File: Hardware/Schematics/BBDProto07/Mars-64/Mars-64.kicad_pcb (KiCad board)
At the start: 4 copper layers, 45.7 x 101.6 mm, 79 parts, among them J101 Conn_Coaxial, J102 Conn_Coaxial, U101 ADG731, U102 ADG731

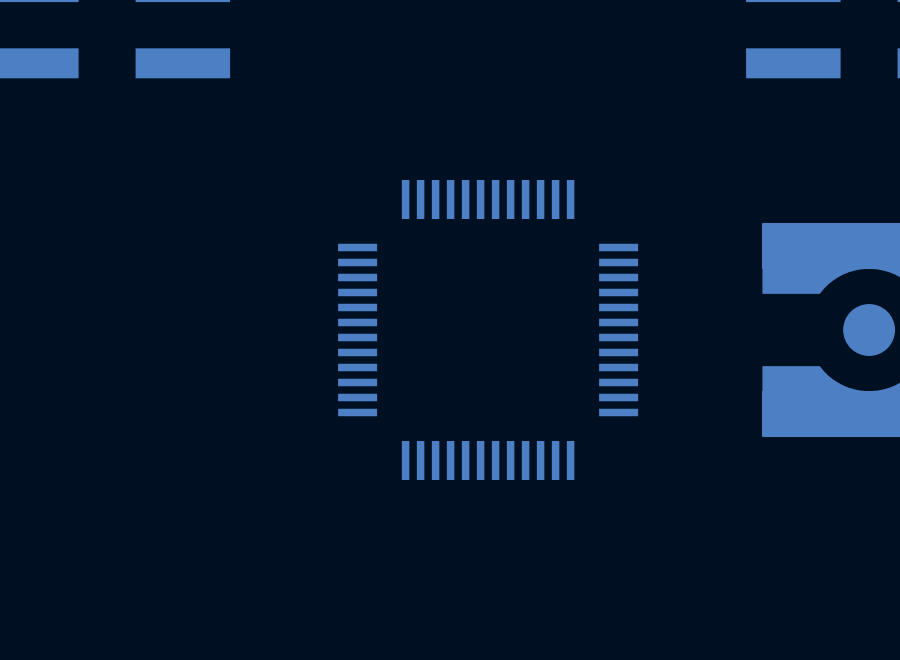
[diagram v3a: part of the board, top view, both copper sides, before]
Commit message: Completed the autorouting for the U101 rotations
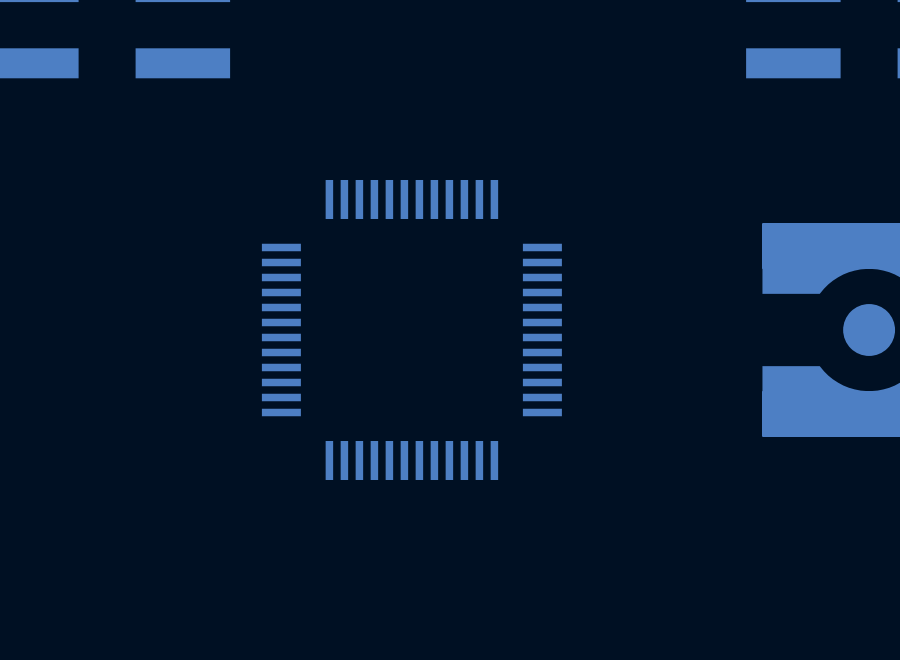
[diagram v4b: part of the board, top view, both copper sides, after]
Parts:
- moved U101 2.54 mm to (78.7, 68.6)
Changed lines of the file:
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@@
   )
   (module Package_QFP:TQFP-48_7x7mm_P0.5mm (layer B.Cu)
-    (at 81.28 68.58 180)
+    (at 78.74 68.58 180)
     (descr "48 LEAD TQFP 7x7mm (see MICREL TQFP7x7-48LD-PL-1.pdf)")
     (tags "QFP 0.5")

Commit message: Added the new fabrication files
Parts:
- turned U102 to 180 degrees
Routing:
- net Net-(JP5-Pad2): track 0.00 -> 204.3 mm
- net /VCC3V3: track 0.00 -> 184.6 mm, vias 0 -> 4
- net /SPI_CLK: track 0.00 -> 184.0 mm, vias 0 -> 2
- net GND: track 0.00 -> 170.6 mm, vias 0 -> 2
- net /SPI_MOSI: track 0.00 -> 139.6 mm
- net /~SPI_CE: track 0.00 -> 134.1 mm
- net Net-(J101-Pad2): track 0.00 -> 124.4 mm, vias 0 -> 2
- net /DB: track 0.00 -> 108.6 mm, vias 0 -> 2
- net Net-(TP204-Pad1): track 0.00 -> 65.9 mm
- net Net-(TP210-Pad1): track 0.00 -> 61.2 mm
- net Net-(TP131-Pad1): track 0.00 -> 60.8 mm, vias 1 -> 2
- net Net-(TP205-Pad1): track 0.00 -> 59.1 mm
- net Net-(TP132-Pad1): track 0.00 -> 58.3 mm
- net Net-(TP208-Pad1): track 0.00 -> 56.4 mm
- net Net-(TP129-Pad1): track 0.00 -> 55.8 mm, vias 1 -> 2
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
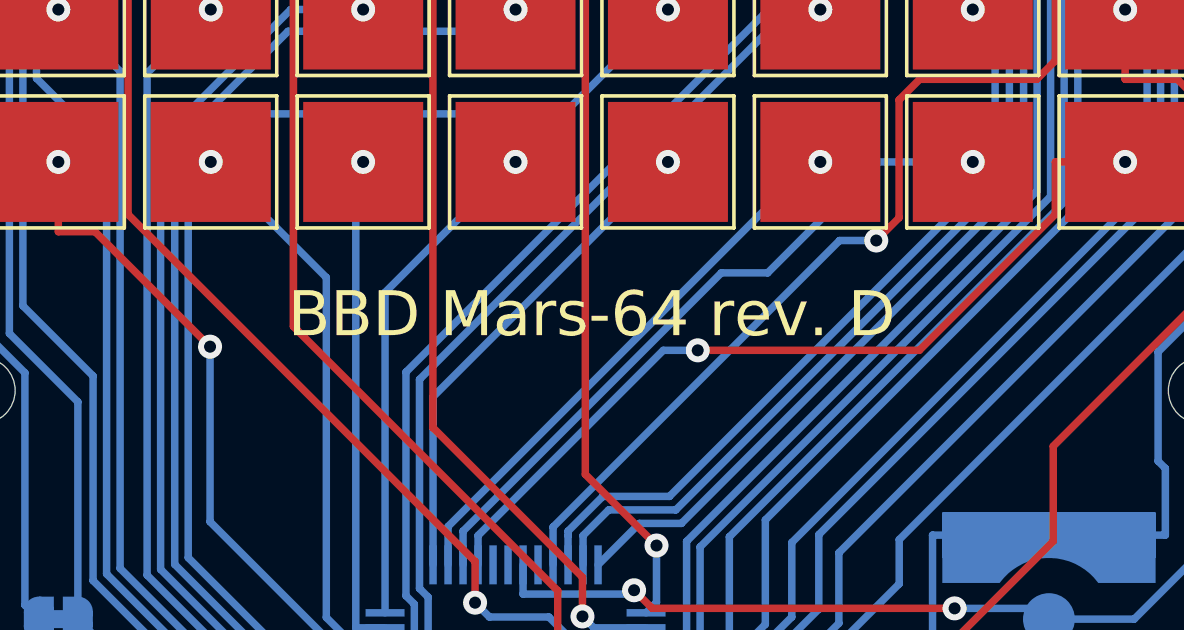
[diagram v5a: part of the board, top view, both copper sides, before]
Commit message: Fixed a few bugs on the PCB and changed the revision from D to E
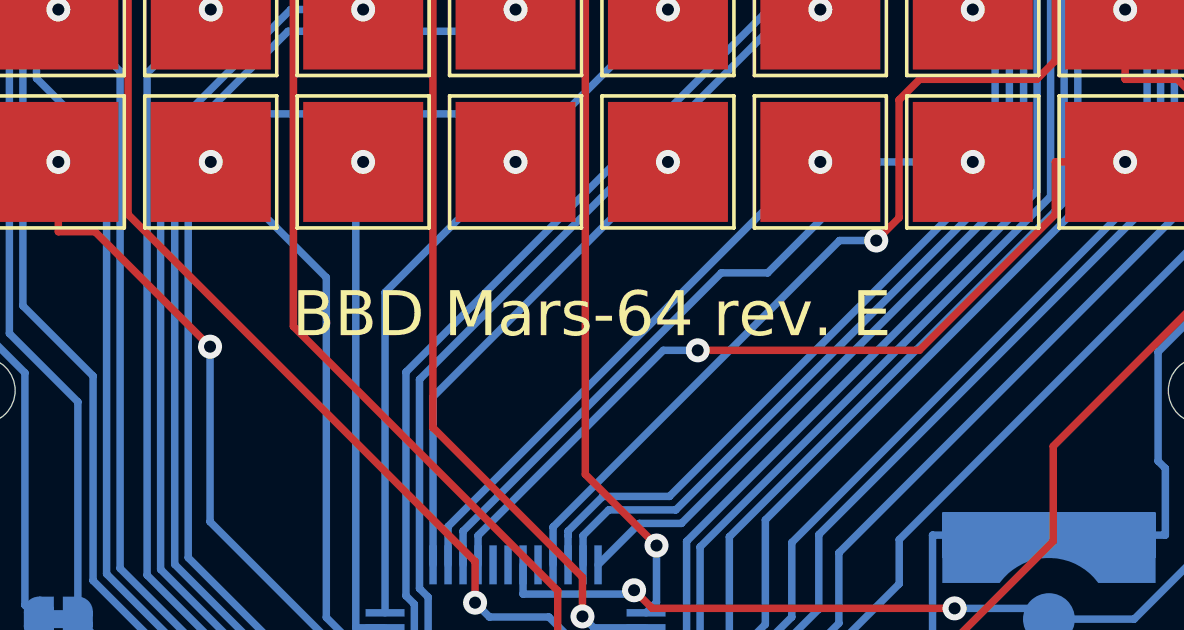
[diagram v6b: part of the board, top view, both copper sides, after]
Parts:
- removed PmodF2: Conn_02x06_Top_Bottom, Mars-64:PinHeader_2x06_P2.54mm_Vertical_SMD_TopBottom_Mirrored
- added PmodF: Conn_02x06_Top_Bottom, Mars-64:PinHeader_2x06_P2.54mm_Vertical_SMD_TopBottom_Mirrored, B.Cu at (68.6, 53.3)
- renumbered J101 to JA, J102 to JB, PmodM1 to PmodM
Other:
- board text added: "3V3"
- board text added: "AGND"
- board text added: "BBD Mars-64 rev. E"
- board text added: "DA"
- board text added: "DB"
- board text added: "GND"
- board text added: "SPI_CE"
- board text added: "SPI_CLK"
- board text added: "SPI_MOSI"
- board text added: "TP11"
- board text added: "TP18"
- board text added: "TP41"
- board text added: "TP48"
- board text added: "TP51"
- board text added: "TP58"
- board text added: "TP81"
- board text added: "TP88"
- board text added: "VSS"
- board text removed: "BBD Mars-64 rev. D"
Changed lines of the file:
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@@
   (general
     (thickness 1.6)
-    (drawings 8)
+    (drawings 29)
     (tracks 882)
     (zones 0)
@@
   (title_block
     (title Mars-64)
-    (date 2020-02-28)
-    (rev D)
+    (date 2020-05-10)
+    (rev E)
     (company "Bio Balance Detector")
   )
   (layers
     (0 F.Cu signal)
-    (1 In1.Cu signal)
+    (1 In1.Cu signal hide)
     (2 In2.Cu signal)
     (31 B.Cu signal)
@@
     (solder_mask_min_width 0.25)
     (aux_axis_origin 0 0)
-    (visible_elements 7FFFFFFF)
+    (visible_elements 7FFF7FFF)
     (pcbplotparams
       (layerselection 0x010fc_ffffffff)
@@
     (tags "SMA SMD Female Jack Vertical")
     (attr smd)
-    (fp_text reference J101 (at 0 4.75) (layer B.SilkS)
+    (fp_text reference JA (at 0 4.75) (layer B.SilkS)
       (effects (font (size 1 1) (thickness 0.15)) (justify mirror))
     )
@@
     (tags "SMA SMD Female Jack Vertical")
     (attr smd)
-    (fp_text reference J102 (at 0 4.75) (layer B.SilkS)
+    (fp_text reference JB (at 0 4.75) (layer B.SilkS)
       (effects (font (size 1 1) (thickness 0.15)) (justify mirror))
     )
@@
     (tags "Surface mounted pin header SMD 2x06 2.54mm double row")
     (attr smd)
-    (fp_text reference PmodM1 (at 0 8.68) (layer B.SilkS)
+    (fp_text reference PmodM (at 0 8.68) (layer B.SilkS)
       (effects (font (size 1 1) (thickness 0.15)) (justify mirror))
     )
@@
     (fp_line (start -1.59 7.62) (end 2.54 7.62) (layer B.Fab) (width 0.1))
     (fp_line (start 2.54 -7.62) (end -2.54 -7.62) (layer B.Fab) (width 0.1))
-    (fp_text user GND (at -6.096 -4.064) (layer B.SilkS)
-      (effects (font (size 1 1) (thickness 0.15)) (justify mirror))
-    )
-    (fp_text user 3V3 (at -6.096 -6.604) (layer B.SilkS)
-      (effects (font (size 1 1) (thickness 0.15)) (justify mirror))
+    (fp_text user GND (at -5.08 -3.81) (layer B.SilkS)
+      (effects (font (size 1 1) (thickness 0.15)) (justify left mirror))
+    )
+    (fp_text user 3V3 (at -5.08 -6.35) (layer B.SilkS)
+      (effects (font (size 1 1) (thickness 0.15)) (justify left mirror))
     )
     (fp_text user 1 (at -3.556 8.128) (layer B.SilkS)
@@
     (tags "Surface mounted pin header SMD 2x06 2.54mm double row")
     (attr smd)
-    (fp_text reference PmodF2 (at 0 8.68) (layer B.SilkS)
+    (fp_text reference PmodF (at 0 8.68) (layer B.SilkS)
       (effects (font (size 1 1) (thickness 0.15)) (justify mirror))
     )
@@
     (fp_line (start 1.59 7.62) (end -2.54 7.62) (layer B.Fab) (width 0.1))
     (fp_line (start -2.54 -7.62) (end 2.54 -7.62) (layer B.Fab) (width 0.1))
-    (fp_text user GND (at 6.096 -4.064) (layer B.SilkS)
-      (effects (font (size 1 1) (thickness 0.15)) (justify mirror))
-    )
-    (fp_text user 3V3 (at 6.096 -6.604) (layer B.SilkS)
-      (effects (font (size 1 1) (thickness 0.15)) (justify mirror))
+    (fp_text user GND (at 5.08 -3.81) (layer B.SilkS)
+      (effects (font (size 1 1) (thickness 0.15)) (justify right mirror))
+    )
+    (fp_text user 3V3 (at 5.08 -6.35) (layer B.SilkS)
+      (effects (font (size 1 1) (thickness 0.15)) (justify right mirror))
     )
     (fp_text user 1 (at 3.556 8.128) (layer B.SilkS)
@@
     )
   )
+  (gr_text TP88 (at 96.52 118.11) (layer B.SilkS)
+    (effects (font (size 1 1) (thickness 0.15)) (justify mirror))
+  )
+  (gr_text TP81 (at 60.96 118.11) (layer B.SilkS)
+    (effects (font (size 1 1) (thickness 0.15)) (justify mirror))
+  )
+  (gr_text TP51 (at 60.96 102.87) (layer B.SilkS)
+    (effects (font (size 1 1) (thickness 0.15)) (justify mirror))
+  )
+  (gr_text TP58 (at 96.52 102.87) (layer B.SilkS)
+    (effects (font (size 1 1) (thickness 0.15)) (justify mirror))
+  )
+  (gr_text TP48 (at 96.52 97.79) (layer B.SilkS)
+    (effects (font (size 1 1) (thickness 0.15)) (justify mirror))
+  )
+  (gr_line (start 78.74 81.28) (end 78.74 121.92) (layer B.SilkS) (width 0.12))
+  (gr_line (start 58.42 101.6) (end 99.06 101.6) (layer B.SilkS) (width 0.12))
+  (gr_text TP41 (at 60.96 97.79) (layer B.SilkS)
+    (effects (font (size 1 1) (thickness 0.15)) (justify mirror))
+  )
+  (gr_text TP18 (at 96.52 82.55) (layer B.SilkS)
+    (effects (font (size 1 1) (thickness 0.15)) (justify mirror))
+  )
+  (gr_text TP11 (at 60.96 82.55) (layer B.SilkS)
+    (effects (font (size 1 1) (thickness 0.15)) (justify mirror))
+  )
+  (gr_text SPI_CE (at 63.5 59.69) (layer B.SilkS)
+    (effects (font (size 1 1) (thickness 0.15)) (justify left mirror))
+  )
+  (gr_text SPI_MOSI (at 63.5 57.15) (layer B.SilkS)
+    (effects (font (size 1 1) (thickness 0.15)) (justify left mirror))
+  )
+  (gr_text SPI_CLK (at 63.5 52.07) (layer B.SilkS)
+    (effects (font (size 1 1) (thickness 0.15)) (justify left mirror))
+  )
+  (gr_text GND (at 63.5 49.53) (layer B.SilkS)
+    (effects (font (size 1 1) (thickness 0.15)) (justify left mirror))
+  )
+  (gr_text 3V3 (at 63.5 46.99) (layer B.SilkS)
+    (effects (font (size 1 1) (thickness 0.15)) (justify left mirror))
+  )
+  (gr_text VSS (at 88.9 59.69) (layer B.SilkS)
+    (effects (font (size 1 1) (thickness 0.15)) (justify left mirror))
+  )
+  (gr_text AGND (at 88.9 57.15) (layer B.SilkS)
+    (effects (font (size 1 1) (thickness 0.15)) (justify left mirror))
+  )
+  (gr_text VSS (at 73.66 59.69) (layer B.SilkS)
+    (effects (font (size 1 1) (thickness 0.15)) (justify right mirror))
+  )
+  (gr_text DA (at 88.9 54.61) (layer B.SilkS)
+    (effects (font (size 1 1) (thickness 0.15)) (justify left mirror))
+  )
+  (gr_text DB (at 88.9 52.07) (layer B.SilkS)
+    (effects (font (size 1 1) (thickness 0.15)) (justify left mirror))
+  )
+  (gr_text AGND (at 73.66 57.15) (layer B.SilkS)
+    (effects (font (size 1 1) (thickness 0.15)) (justify right mirror))
+  )
   (dimension 101.6 (width 0.15) (layer Dwgs.User)
     (gr_text "101.600 mm" (at 107.98 93.98 270) (layer Dwgs.User)
@@
     (arrow2b (pts (xy 55.88 38.1) (xy 57.006504 37.513579)))
   )
-  (gr_text "BBD Mars-64 rev. D" (at 78.74 124.46) (layer F.SilkS)
+  (gr_text "BBD Mars-64 rev. E" (at 78.74 124.46) (layer F.SilkS)
     (effects (font (size 1.5 1.5) (thickness 0.3)))
   )
-  (gr_text "BBD Mars-64 rev. D" (at 78.74 124.46) (layer B.SilkS)
+  (gr_text "BBD Mars-64 rev. E" (at 78.74 124.46) (layer B.SilkS)
     (effects (font (size 1.5 1.5) (thickness 0.3)) (justify mirror))
   )

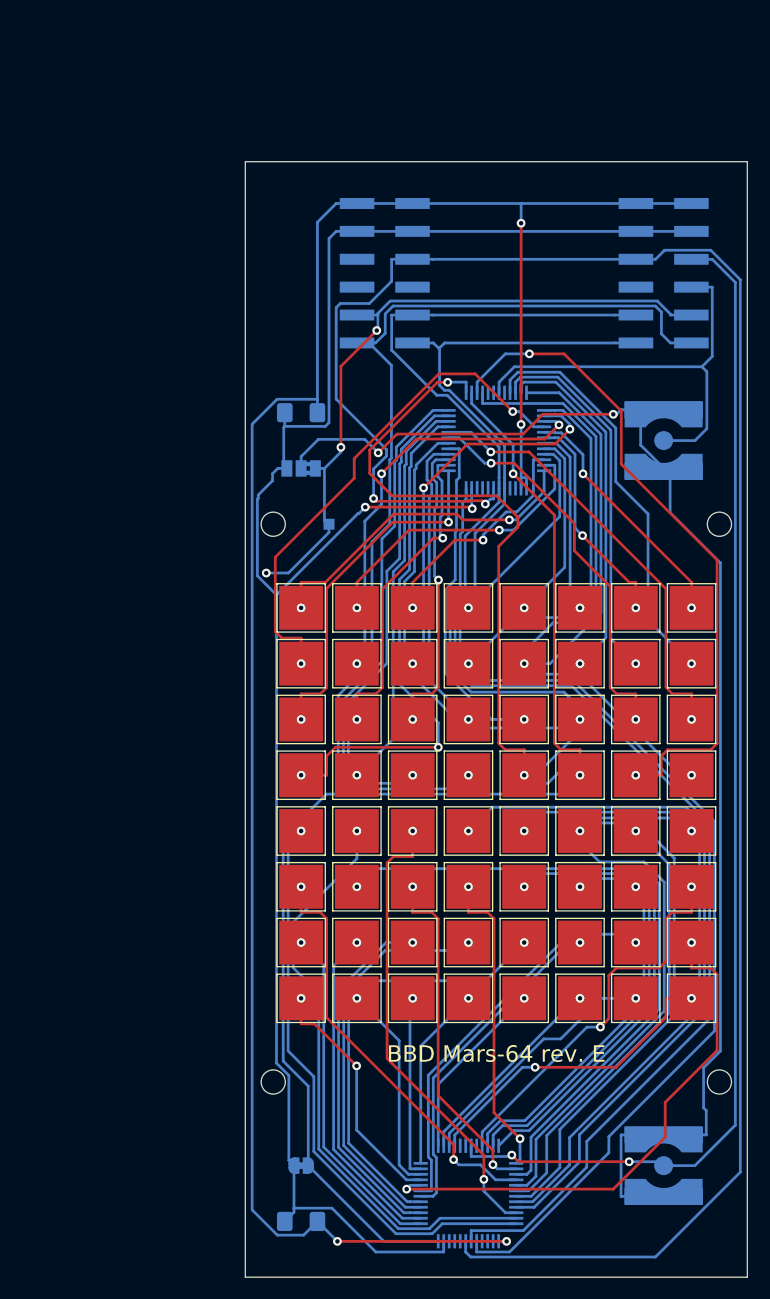
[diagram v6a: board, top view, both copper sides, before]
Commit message: Fixed the footprints of PmodF and PmodM, and removed the routed tracks
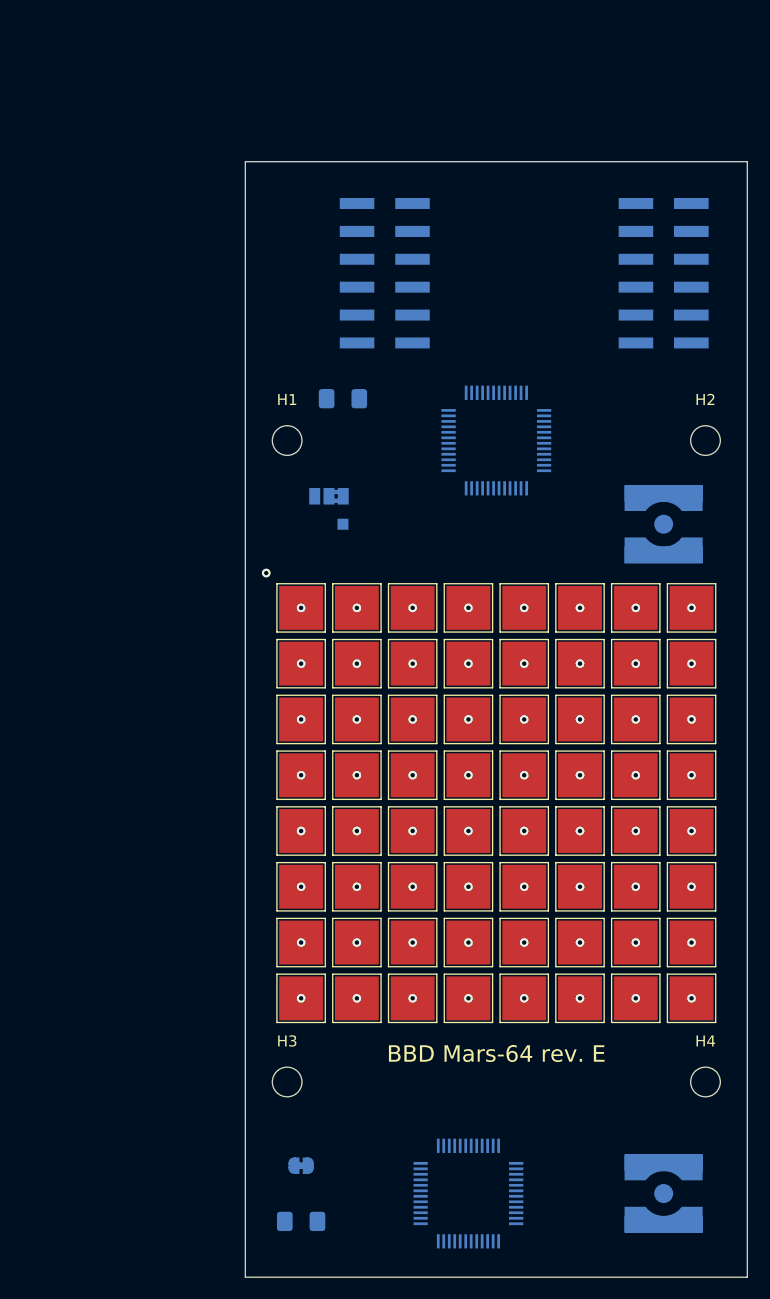
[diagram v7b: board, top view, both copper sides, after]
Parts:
- removed the PmodF at (68.6, 53.3)
- removed the PmodM at (94.0, 53.3)
- added PmodF: Conn_02x06_Top_Bottom, Mars-64:PinHeader_2x06_P2.54mm_Vertical_SMD_TopBottom, B.Cu at (68.6, 53.3)
- added PmodM: Conn_02x06_Top_Bottom, Mars-64:PinHeader_2x06_P2.54mm_Vertical_SMD_TopBottom_Mirrored, B.Cu at (94.0, 53.3)
- H1, H2, H3, H4: footprint MountingHole:MountingHole_2.2mm_M2 -> MountingHole:MountingHole_2.7mm_M2.5
- moved H1 7.73 mm to (59.7, 68.6)
- moved H2 7.73 mm to (97.8, 68.6)
- moved JA 7.62 mm to (94.0, 76.2)
- moved C1 4.02 mm to (64.8, 64.8)
- moved JP4 3.59 mm to (63.5, 73.7)
- moved JB 2.54 mm to (94.0, 137.2)
- moved H3 1.27 mm to (59.7, 127.0)
- moved H4 1.27 mm to (97.8, 127.0)
- moved TPAGND1 1.27 mm to (64.8, 76.2)
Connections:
- net Net-(JP5-Pad2) renamed /VSS
- U101 pad 15: (no net) -> Net-(U101-Pad15)
- U101 pad 16: (no net) -> Net-(U101-Pad16)
- U101 pad 20: (no net) -> Net-(U101-Pad20)
- U101 pad 21: (no net) -> Net-(U101-Pad21)
- U101 pad 22: (no net) -> Net-(U101-Pad22)
- U101 pad 41: (no net) -> Net-(U101-Pad41)
- U101 pad 42: (no net) -> Net-(U101-Pad42)
- U101 pad 44: (no net) -> Net-(U101-Pad44)
- U102 pad 15: (no net) -> Net-(U102-Pad15)
- U102 pad 16: (no net) -> Net-(U102-Pad16)
- U102 pad 20: (no net) -> Net-(U102-Pad20)
- U102 pad 21: (no net) -> Net-(U102-Pad21)
- U102 pad 22: (no net) -> Net-(U102-Pad22)
- U102 pad 41: (no net) -> Net-(U102-Pad41)
- U102 pad 42: (no net) -> Net-(U102-Pad42)
- U102 pad 44: (no net) -> Net-(U102-Pad44)
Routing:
- net /VSS: track 204.3 -> 0.00 mm
- net /VCC3V3: track 184.6 -> 0.00 mm, vias 4 -> 0
- net /SPI_CLK: track 184.0 -> 0.00 mm, vias 2 -> 0
- net GND: track 170.6 -> 0.00 mm, vias 2 -> 0
- net /SPI_MOSI: track 139.6 -> 0.00 mm
- net /~SPI_CE: track 134.1 -> 0.00 mm
- net Net-(J101-Pad2): track 124.4 -> 0.00 mm, vias 2 -> 0
- net /DB: track 108.6 -> 0.00 mm, vias 2 -> 0
- net Net-(TP204-Pad1): track 65.9 -> 0.00 mm
- net /AGND: track 61.8 -> 0.00 mm, vias 3 -> 1
- net Net-(TP210-Pad1): track 61.2 -> 0.00 mm
- net Net-(TP131-Pad1): track 60.8 -> 0.00 mm, vias 2 -> 1
- net Net-(TP205-Pad1): track 59.1 -> 0.00 mm
- net Net-(TP132-Pad1): track 58.3 -> 0.00 mm
- net Net-(TP208-Pad1): track 56.4 -> 0.00 mm
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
